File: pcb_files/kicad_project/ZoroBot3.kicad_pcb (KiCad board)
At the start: 2 copper layers, 67.6 x 91.9 mm, 178 parts, among them Q1 NMOS, Q2 AON7423, Q3 ST-1KL3A, Q4 ST-1KL3A, Q5 ST-1KL3A, Q6 ST-1KL3A, U1 MPU-6500, U2 MPU-6500, Y1 Crystal

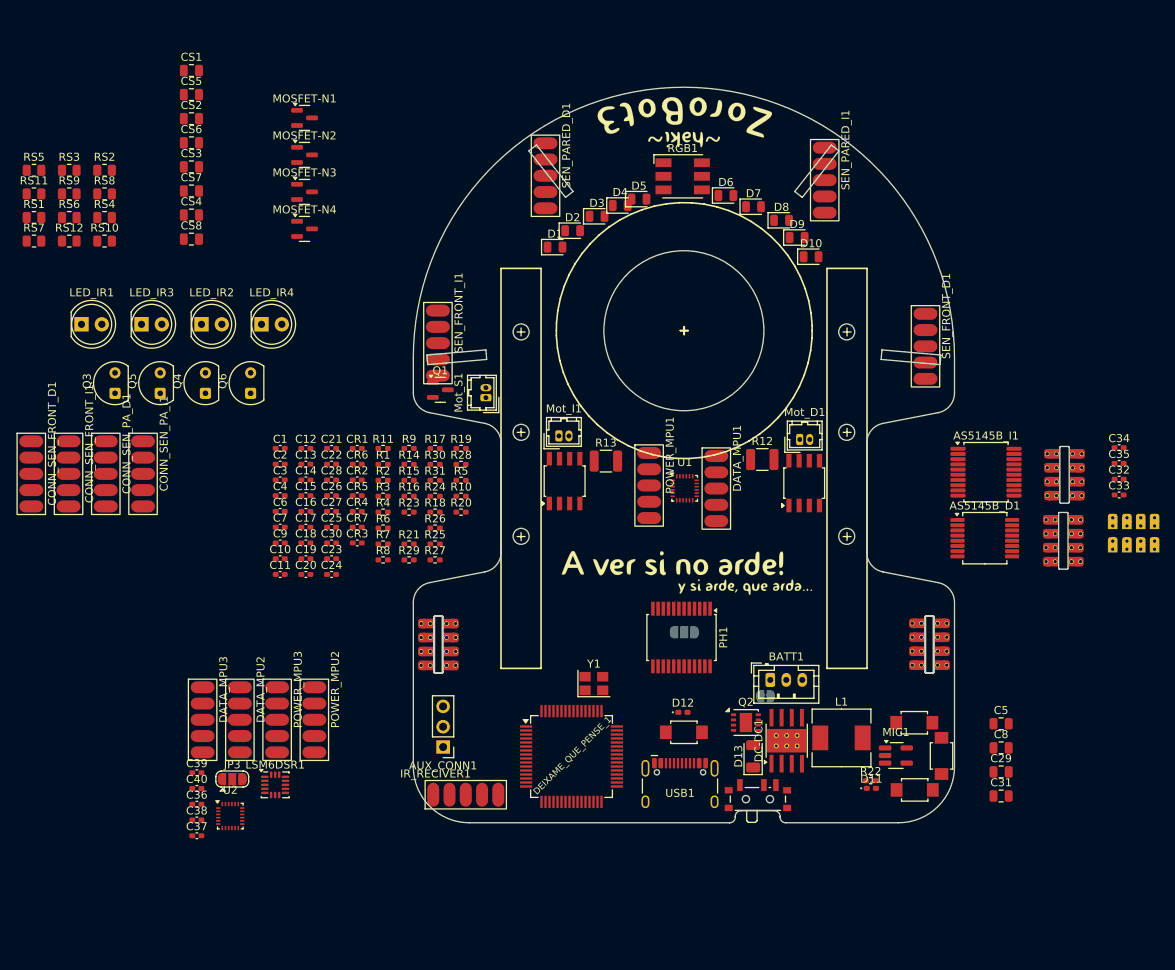
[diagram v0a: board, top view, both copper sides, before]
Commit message: Corrige errores de esquematico, crea las PCBs auxiliares, y posiciona todos los elementos para comenzar el ruteado.
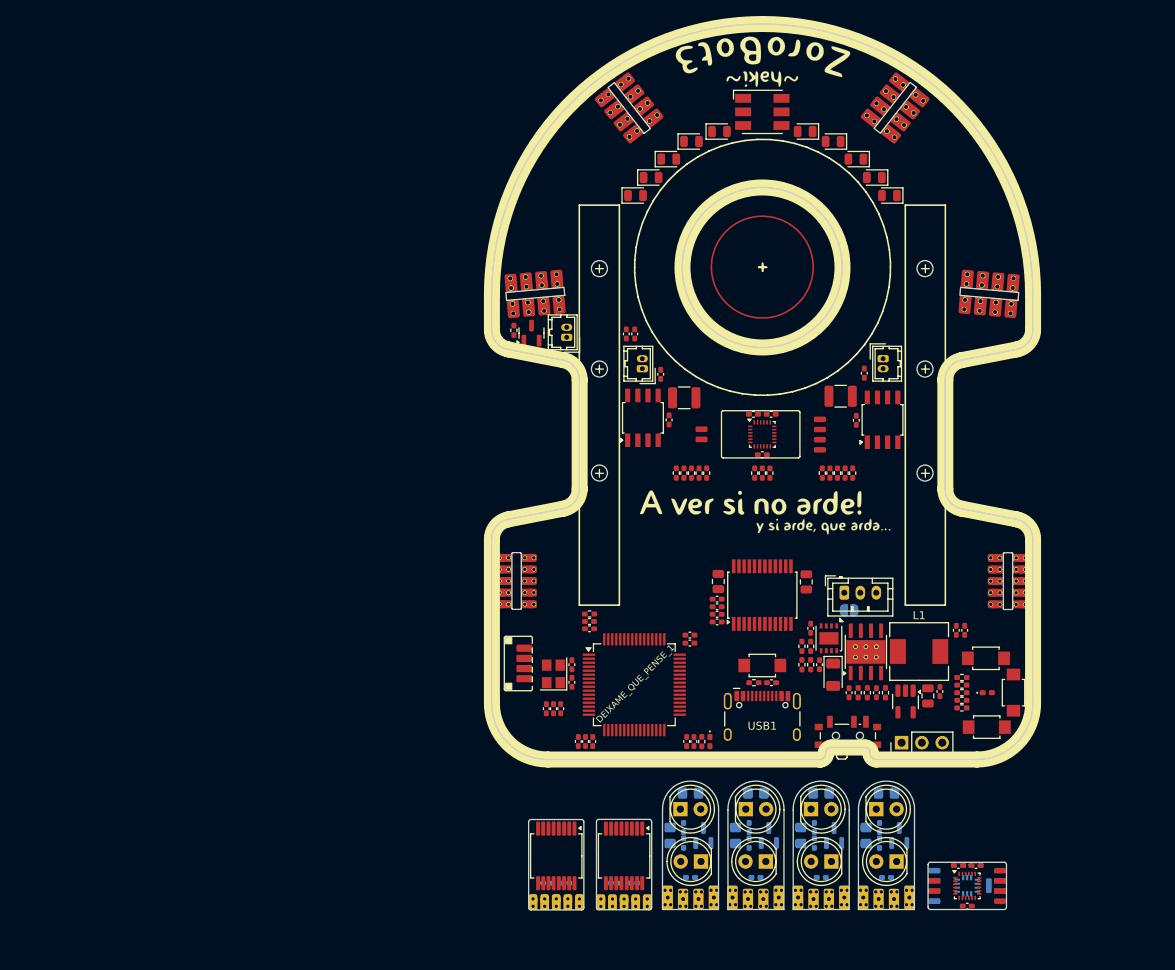
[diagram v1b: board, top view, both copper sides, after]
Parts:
- removed ENC_L1, ENC_R1: Conn_01x05_Socket, custom_footprints:FujitoraBot2_PCBmain_Encoder
- removed JP1: SolderJumper_3_Open, Jumper:SolderJumper-3_P1.3mm_Open_RoundedPad1.0x1.5mm
- AS5145B_I1: footprint Package_SO:SSOP-20_5.3x7.2mm_P0.65mm -> Package_SO:SSOP-16_5.3x6.2mm_P0.65mm
- C28: value 10uF -> 0.1uf
- C29: value 47uF -> 0.1uF; footprint Capacitor_SMD:C_0805_2012Metric -> Capacitor_SMD:C_0402_1005Metric_Pad0.74x0.62mm_HandSolder
- C32, C33, C34, C35, C37, C38, MOSFET-N1, MOSFET-N2, MOSFET-N3, MOSFET-N4: moved to B.Cu
- CONN_SEN_FRONT_D1, CONN_SEN_FRONT_I1, CONN_SEN_PA_D1, CONN_SEN_PA_I1: footprint custom_footprints:1x05 Pad -> custom_footprints:ZoroBot3_Sensors
- CS1, CS2, CS3, CS4, CS5, CS6, CS7, CS8: footprint Capacitor_SMD:C_0805_2012Metric -> Capacitor_SMD:C_0402_1005Metric_Pad0.74x0.62mm_HandSolder; moved to B.Cu
- DATA_MPU1, DATA_MPU3: footprint custom_footprints:1x05 Pad -> custom_footprints:ZoroBot3_Data_MPU
- DATA_MPU2: footprint custom_footprints:1x05 Pad -> custom_footprints:ZoroBot3_Data_MPU; moved to B.Cu
- ENC_D1, ENC_I1: footprint custom_footprints:FujitoraBot2_PCBmain_Encoder -> custom_footprints:ZoroBot3_PCBmain_Encoder
- ENC_D_CONN1, ENC_I_CONN1: footprint custom_footprints:FujitoraBot2_PCBmodule_encoder -> custom_footprints:ZoroBot3_PCBmodule_encoder
- IR_RECIVER1: footprint custom_footprints:1x05 Pad -> custom_footprints:IR_SENSOR_SMD_TSSP77038ETR
- JP3: value SolderJumper_3_Open -> Conn_01x01_Pin; footprint Jumper:SolderJumper-3_P1.3mm_Open_RoundedPad1.0x1.5mm -> custom_footprints:Generic_simple_1x_SMD_pin; moved to B.Cu
- LED_IR1, LED_IR2, LED_IR3, LED_IR4: footprint LED_THT:LED_D5.0mm -> LED_THT:LED_D5.0mm_Clear
- LSM6DSR1: footprint Sensor_Motion:Analog_LGA-16_3.25x3mm_P0.5mm_LayoutBorder3x5y -> Package_LGA:Bosch_LGA-14_3x2.5mm_P0.5mm; moved to B.Cu
- Mot_D1, Mot_I1, Mot_S1: footprint Connector_Hirose:Hirose_DF13-02P-1.25DSA_1x02_P1.25mm_Vertical -> custom_footprints:Connector_motor_1.25_Hirose_DF13-02P-1.25DSA_1x02_P1.25mm_Vertical
- POWER_MPU1, POWER_MPU2: footprint custom_footprints:1x05 Pad -> custom_footprints:ZoroBot3_Power_MPU
- POWER_MPU3: footprint custom_footprints:1x05 Pad -> custom_footprints:ZoroBot3_Power_MPU; moved to B.Cu
- Q3, Q4, Q5, Q6: footprint OptoDevice:Osram_SFH205 -> LED_THT:LED_D5.0mm_IRBlack
- RS1, RS10, RS2, RS3, RS4, RS7, RS8, RS9: footprint Resistor_SMD:R_0805_2012Metric -> Resistor_SMD:R_0805_2012Metric_Pad1.20x1.40mm_HandSolder; moved to B.Cu
- RS11, RS12, RS5, RS6: footprint Resistor_SMD:R_0805_2012Metric -> Resistor_SMD:R_0402_1005Metric_Pad0.72x0.64mm_HandSolder; moved to B.Cu
- SEN_FRONT_D1, SEN_FRONT_I1, SEN_PARED_D1, SEN_PARED_I1: footprint custom_footprints:1x05 Pad -> custom_footprints:ZoroBot3_Main_sensors
- Y1: value Crystal -> Crystal_GND24
- moved RS5 135.1 mm to (165.8, 134.4), turned to 90 degrees
- moved RS3 129.7 mm to (164.1, 133.4), turned to 90 degrees
- moved CS2 128.6 mm to (166.6, 138.7), turned to 180 degrees
- moved RS1 128.6 mm to (166.6, 128.2)
- moved CS1 127.9 mm to (165.8, 132.4), turned to -90 degrees
- moved RS11 126.9 mm to (157.6, 134.4), turned to 90 degrees
- moved RS9 121.6 mm to (155.9, 133.4), turned to 90 degrees
- moved CS6 121.0 mm to (158.5, 138.7), turned to 180 degrees
- moved CS5 120.2 mm to (157.6, 132.4), turned to -90 degrees
- moved RS7 120.2 mm to (158.5, 128.2)
- moved MOSFET-N1 116.5 mm to (168.2, 133.4), turned to 90 degrees
- moved LED_IR1 116.4 mm to (165.3, 130.2)
- moved CONN_SEN_FRONT_D1 115.6 mm to (159.6, 141.2)
- moved CONN_SEN_PA_D1 114.5 mm to (167.8, 141.2)
- moved Q3 113.9 mm to (167.9, 136.7), turned to 180 degrees
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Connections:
- CS1 pad 1: Net-(LED_IR1-A) -> /Sensores/3.3_D
- CS3 pad 1: Net-(LED_IR2-A) -> /Sensores/3.3_I
- CS5 pad 1: Net-(LED_IR3-A) -> /Sensores/3.3_FD
- CS7 pad 1: Net-(LED_IR4-A) -> /Sensores/3.3_FI
- JP3 pad 1: /Giroscopio/GND_MPU -> Net-(JP3-Pin_1)
- LSM6DSR1 pad 2: Net-(JP3-C) -> Net-(JP3-Pin_1)
- LSM6DSR1 pad 3: Net-(JP3-C) -> Net-(JP3-Pin_1)
- PH1 pad 6: Net-(JP1-C) -> +3V3
- Y1 pad 2: Net-(DEIXAME_QUE_PENSE_1-PH0/OSC_IN) -> GND
- Y1 pad 3: (no net) -> Net-(DEIXAME_QUE_PENSE_1-PH0/OSC_IN)
- Y1 pad 4: (no net) -> GND
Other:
- board size 67.6 x 91.9 mm -> 67.6 x 110.7 mm
- board text added: "Component"
- board text added: "Directly Below"
- board text added: "KEEPOUT"
- board text added: "No Copper"

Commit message: Finaliza el diseño de la PCB de ZoroBot3 Rebuild y añade gerbers y BOM
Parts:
- removed C14, C16: 0.1uF, Capacitor_SMD:C_0402_1005Metric_Pad0.74x0.62mm_HandSolder
- added C41: 10uF, Capacitor_SMD:C_0402_1005Metric_Pad0.74x0.62mm_HandSolder, F.Cu at (144.9, 119.4)
- added C42: 10uF, Capacitor_SMD:C_0402_1005Metric_Pad0.74x0.62mm_HandSolder, F.Cu at (144.9, 120.4)
- added C43: 10uF, Capacitor_SMD:C_0402_1005Metric_Pad0.74x0.62mm_HandSolder, F.Cu at (144.9, 121.4)
- added C44: 10uF, Capacitor_SMD:C_0402_1005Metric_Pad0.74x0.62mm_HandSolder, F.Cu at (170.6, 137.1)
- added C45: 10uF, Capacitor_SMD:C_0402_1005Metric_Pad0.74x0.62mm_HandSolder, F.Cu at (170.6, 135.2)
- added C46: 10uF, Capacitor_SMD:C_0402_1005Metric_Pad0.74x0.62mm_HandSolder, F.Cu at (170.6, 136.2)
- added C47: 10uF, Capacitor_SMD:C_0402_1005Metric_Pad0.74x0.62mm_HandSolder, F.Cu at (173.0, 124.9)
- added C48: 10uF, Capacitor_SMD:C_0402_1005Metric_Pad0.74x0.62mm_HandSolder, F.Cu at (170.9, 124.9)
- added C49: 10uF, Capacitor_SMD:C_0402_1005Metric_Pad0.74x0.62mm_HandSolder, F.Cu at (172.0, 124.9)
- added C50: 10uF, Capacitor_SMD:C_0402_1005Metric_Pad0.74x0.62mm_HandSolder, F.Cu at (168.9, 124.9)
- added C51: 10uF, Capacitor_SMD:C_0402_1005Metric_Pad0.74x0.62mm_HandSolder, F.Cu at (169.9, 124.9)
- added C52: 10uF, Capacitor_SMD:C_0402_1005Metric_Pad0.74x0.62mm_HandSolder, F.Cu at (170.6, 138.1)
- added kibuzzard-6779A98A: G***, kibuzzard-6779A98A, B.Cu at (110.8, 99.0)
- added kibuzzard-6779A9B1: G***, kibuzzard-6779A9B1, B.Cu at (185.3, 98.9)
- added kibuzzard-677A7C8F: G***, kibuzzard-677A7C8F, F.Cu at (155.8, 62.7)
- added kibuzzard-677A7C9A: G***, kibuzzard-677A7C9A, F.Cu at (159.0, 64.0)
- added kibuzzard-677A7CA3: G***, kibuzzard-677A7CA3, F.Cu at (161.9, 65.9)
- added kibuzzard-677A7CAF: G***, kibuzzard-677A7CAF, F.Cu at (164.4, 68.3)
- added kibuzzard-677A7CBB: G***, kibuzzard-677A7CBB, F.Cu at (166.3, 71.2)
- added kibuzzard-677A7D71: G***, kibuzzard-677A7D71, F.Cu at (136.8, 68.3)
- added kibuzzard-677A7D7B: G***, kibuzzard-677A7D7B, F.Cu at (139.2, 65.9)
- added kibuzzard-677A7D86: G***, kibuzzard-677A7D86, F.Cu at (142.1, 64.0)
- added kibuzzard-677A7E2E: G***, kibuzzard-677A7E2E, F.Cu at (134.8, 71.2)
- added kibuzzard-677A7E3B: G***, kibuzzard-677A7E3B, F.Cu at (145.3, 62.7)
- AS5145B_D1, AS5145B_I1: footprint Package_SO:SSOP-16_5.3x6.2mm_P0.65mm -> custom_footprints:Encoder_AS5145B
- BATT1: footprint Connector_JST:JST_PH_B3B-PH-K_1x03_P2.00mm_Vertical -> Connector_JST:JST_XH_B3B-XH-A_1x03_P2.50mm_Vertical
- C37, C38, DATA_MPU2, JP3, LSM6DSR1, POWER_MPU3: moved to F.Cu
- CR4, CR7: footprint Capacitor_SMD:C_0402_1005Metric_Pad0.74x0.62mm_HandSolder -> Capacitor_SMD:C_0603_1608Metric
- CR6: value 0.1uF -> 47uF; footprint Capacitor_SMD:C_0402_1005Metric_Pad0.74x0.62mm_HandSolder -> Capacitor_SMD:C_1206_3216Metric
- D13: footprint Diode_SMD:D_1206_3216Metric -> Diode_SMD:D_0805_2012Metric_Pad1.15x1.40mm_HandSolder
- MOSFET-N1, MOSFET-N2, MOSFET-N3, MOSFET-N4: value AO3401 -> AO3400 (A09T)
- R12, R13: footprint Resistor_SMD:R_1210_3225Metric -> Resistor_SMD:R_2512_6332Metric
- moved DATA_MPU3 79.3 mm to (113.3, 98.1), turned to 90 degrees
- moved C40 77.5 mm to (110.3, 102.2), turned to 90 degrees
- moved POWER_MPU3 75.3 mm to (113.3, 106.3), turned to 90 degrees
- moved U2 73.7 mm to (113.3, 102.2), turned to -90 degrees
- moved C39 71.3 mm to (116.4, 101.0), turned to 90 degrees
- moved C36 68.3 mm to (116.4, 103.2), turned to -90 degrees
- moved C33 65.4 mm to (178.9, 103.4), turned to 180 degrees
- moved AS5145B_D1 64.2 mm to (178.9, 100.7)
- moved ENC_D_CONN1 63.6 mm to (178.9, 106.3)
- moved C32 63.1 mm to (178.9, 104.4)
- moved RS9 62.5 mm to (188.2, 79.9)
- moved CONN_SEN_PA_I1 62.3 mm to (111.2, 87.8)
- moved MOSFET-N2 62.2 mm to (112.2, 79.9)
- moved LED_IR3 62.1 mm to (188.6, 76.6)
- moved RS7 62.1 mm to (189.9, 74.6)
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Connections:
- AD8418AWBZ_2 pad 1: /SHUNT_MI -> /MOT_I-
- AD8418AWBZ_2 pad 8: /MOT_I+ -> /SHUNT_MI
- C36 pad 1: /Giroscopio/GND_MPU -> /Giroscopio/GND_MPU_A
- C36 pad 2: /Giroscopio/3.3_MPU -> /Giroscopio/3.3_MPU_A
- C37 pad 1: /Giroscopio/GND_MPU -> /Giroscopio/GND_MPU_B
- C37 pad 2: /Giroscopio/3.3_MPU -> /Giroscopio/3.3_MPU_B
- C38 pad 1: /Giroscopio/GND_MPU -> /Giroscopio/GND_MPU_B
- C38 pad 2: /Giroscopio/3.3_MPU -> /Giroscopio/3.3_MPU_B
- C39 pad 1: /Giroscopio/GND_MPU -> /Giroscopio/GND_MPU_A
- C39 pad 2: /Giroscopio/3.3_MPU -> /Giroscopio/3.3_MPU_A
- C40 pad 1: /Giroscopio/GND_MPU -> /Giroscopio/GND_MPU_A
- DATA_MPU2 pad 1: /Giroscopio/SPI_MISO_CONN -> /Giroscopio/SPI_MISO_CONN_B
- DATA_MPU2 pad 2: /Giroscopio/SPI_MOSI_CONN -> /Giroscopio/SPI_MOSI_CONN_B
- DATA_MPU2 pad 3: /Giroscopio/SPI_SCK_CONN -> /Giroscopio/SPI_SCK_CONN_B
- DATA_MPU2 pad 4: /Giroscopio/SPI_NSS_CONN -> /Giroscopio/SPI_NSS_CONN_B
- DATA_MPU3 pad 1: /Giroscopio/SPI_MISO_CONN -> /Giroscopio/SPI_MISO_CONN_A
- DATA_MPU3 pad 2: /Giroscopio/SPI_MOSI_CONN -> /Giroscopio/SPI_MOSI_CONN_A
- DATA_MPU3 pad 3: /Giroscopio/SPI_SCK_CONN -> /Giroscopio/SPI_SCK_CONN_A
- DATA_MPU3 pad 4: /Giroscopio/SPI_NSS_CONN -> /Giroscopio/SPI_NSS_CONN_A
- DEIXAME_QUE_PENSE_1 pad 54: /ENC_2_I -> /ENC_D_I
- DEIXAME_QUE_PENSE_1 pad 55: /ENC_1_I -> /ENC_I_I
- DEIXAME_QUE_PENSE_1 pad 56: /ENC_2_B -> /ENC_D_B
- DEIXAME_QUE_PENSE_1 pad 57: /ENC_2_A -> /ENC_D_A
- DEIXAME_QUE_PENSE_1 pad 58: /ENC_1_B -> /ENC_I_B
- DEIXAME_QUE_PENSE_1 pad 59: /ENC_1_A -> /ENC_I_A
- ENC_D1 pad 3: /ENC_1_A -> /ENC_D_I
- ENC_D1 pad 4: /ENC_1_B -> /ENC_D_A
- ENC_D1 pad 5: /ENC_1_I -> /ENC_D_B
- ENC_D_CONN1 pad 3: /Encoders/ENC_D_A_CONN -> /Encoders/ENC_D_I_CONN
- ENC_D_CONN1 pad 4: /Encoders/ENC_D_B_CONN -> /Encoders/ENC_D_A_CONN
- ENC_D_CONN1 pad 5: /Encoders/ENC_D_I_CONN -> /Encoders/ENC_D_B_CONN
- ENC_I1 pad 3: /ENC_2_A -> /ENC_I_I
- ENC_I1 pad 4: /ENC_2_B -> /ENC_I_A
- ENC_I1 pad 5: /ENC_2_I -> /ENC_I_B
- ENC_I_CONN1 pad 3: /Encoders/ENC_I_A_CONN -> /Encoders/ENC_I_I_CONN
- ENC_I_CONN1 pad 4: /Encoders/ENC_I_B_CONN -> /Encoders/ENC_I_A_CONN
- ENC_I_CONN1 pad 5: /Encoders/ENC_I_I_CONN -> /Encoders/ENC_I_B_CONN
- LSM6DSR1 pad 1: /Giroscopio/SPI_MISO_CONN -> /Giroscopio/SPI_MISO_CONN_B
- LSM6DSR1 pad 12: /Giroscopio/SPI_NSS_CONN -> /Giroscopio/SPI_NSS_CONN_B
- LSM6DSR1 pad 13: /Giroscopio/SPI_SCK_CONN -> /Giroscopio/SPI_SCK_CONN_B
- LSM6DSR1 pad 14: /Giroscopio/SPI_MOSI_CONN -> /Giroscopio/SPI_MOSI_CONN_B
- LSM6DSR1 pad 5: /Giroscopio/3.3_MPU -> /Giroscopio/3.3_MPU_B
- LSM6DSR1 pad 6: /Giroscopio/GND_MPU -> /Giroscopio/GND_MPU_B
- LSM6DSR1 pad 7: /Giroscopio/GND_MPU -> /Giroscopio/GND_MPU_B
- LSM6DSR1 pad 8: /Giroscopio/3.3_MPU -> /Giroscopio/3.3_MPU_B
- MOSFET-N1 pad 1: /Sensores/EMI_PA_D_CONN -> Net-(LED_IR1-K)
- MOSFET-N1 pad 2: /Sensores/GND_D -> /Sensores/EMI_PA_D_CONN
- MOSFET-N1 pad 3: Net-(LED_IR1-K) -> /Sensores/GND_D
- MOSFET-N2 pad 1: /Sensores/EMI_PA_I_CONN -> Net-(LED_IR2-K)
- MOSFET-N2 pad 2: /Sensores/GND_I -> /Sensores/EMI_PA_I_CONN
- MOSFET-N2 pad 3: Net-(LED_IR2-K) -> /Sensores/GND_I
- MOSFET-N3 pad 1: /Sensores/EMI_FRONT_D_CONN -> Net-(LED_IR3-K)
- MOSFET-N3 pad 2: /Sensores/GND_FD -> /Sensores/EMI_FRONT_D_CONN
- MOSFET-N3 pad 3: Net-(LED_IR3-K) -> /Sensores/GND_FD
- MOSFET-N4 pad 1: /Sensores/EMI_FRONT_I_CONN -> Net-(LED_IR4-K)
- MOSFET-N4 pad 2: /Sensores/GND_FI -> /Sensores/EMI_FRONT_I_CONN
- MOSFET-N4 pad 3: Net-(LED_IR4-K) -> /Sensores/GND_FI
- PH1 pad 1: /BATT -> /SHUNT_MD
- PH1 pad 10: /MOT_I_PWM -> GND
- PH1 pad 11: /BATT -> /SHUNT_MI
- PH1 pad 12: /BATT -> /SHUNT_MI
- PH1 pad 13: /SHUNT_MI -> /BATT
- PH1 pad 14: /SHUNT_MI -> /BATT
- PH1 pad 15: GND -> /MOT_I_PWM
- PH1 pad 16: GND -> /MOT_I_B
- PH1 pad 17: /MOT_I- -> /MOT_I_A
- PH1 pad 18: /MOT_I- -> GND
- PH1 pad 19: /MOT_D- -> +3V3
- PH1 pad 2: /MOT_D_PWM -> /SHUNT_MD
- PH1 pad 20: /MOT_D- -> +3V3
- PH1 pad 21: GND -> /MOT_D_B
- PH1 pad 22: GND -> /MOT_D_A
- PH1 pad 23: /SHUNT_MD -> /MOT_D_PWM
- PH1 pad 24: /SHUNT_MD -> /BATT
- PH1 pad 3: /MOT_D_A -> GND
- PH1 pad 4: /MOT_D_B -> GND
- PH1 pad 5: +3V3 -> /MOT_D-
- PH1 pad 6: +3V3 -> /MOT_D-
- PH1 pad 7: GND -> /MOT_I+
- PH1 pad 8: /MOT_I_A -> /MOT_I+
- PH1 pad 9: /MOT_I_B -> GND
- POWER_MPU2 pad 1: /Giroscopio/GND_MPU -> /Giroscopio/GND_MPU_B
- POWER_MPU2 pad 2: /Giroscopio/3.3_MPU -> /Giroscopio/3.3_MPU_B
- POWER_MPU3 pad 1: /Giroscopio/GND_MPU -> /Giroscopio/GND_MPU_A
- POWER_MPU3 pad 2: /Giroscopio/3.3_MPU -> /Giroscopio/3.3_MPU_A
- POWER_SWITCH1 pad 1: unconnected-(POWER_SWITCH1-A-Pad1) -> Net-(POWER_SWITCH1-A)
- POWER_SWITCH1 pad 3: Net-(POWER_SWITCH1-C) -> unconnected-(POWER_SWITCH1-C-Pad3)
- R13 pad 1: /MOT_I+ -> /MOT_I-
- R27 pad 1: Net-(POWER_SWITCH1-C) -> Net-(POWER_SWITCH1-A)
- R28 pad 1: Net-(POWER_SWITCH1-C) -> Net-(POWER_SWITCH1-A)
- U2 pad 13: /Giroscopio/3.3_MPU -> /Giroscopio/3.3_MPU_A
- U2 pad 18: /Giroscopio/GND_MPU -> /Giroscopio/GND_MPU_A
- U2 pad 20: /Giroscopio/GND_MPU -> /Giroscopio/GND_MPU_A
- U2 pad 22: /Giroscopio/SPI_NSS_CONN -> /Giroscopio/SPI_NSS_CONN_A
- U2 pad 23: /Giroscopio/SPI_SCK_CONN -> /Giroscopio/SPI_SCK_CONN_A
- U2 pad 24: /Giroscopio/SPI_MOSI_CONN -> /Giroscopio/SPI_MOSI_CONN_A
- U2 pad 8: /Giroscopio/3.3_MPU -> /Giroscopio/3.3_MPU_A
- U2 pad 9: /Giroscopio/SPI_MISO_CONN -> /Giroscopio/SPI_MISO_CONN_A
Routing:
- net +3V3: track 0.00 -> 804.2 mm, vias 0 -> 35
- net GND: track 0.00 -> 289.1 mm, vias 0 -> 130
- net +5V: track 0.00 -> 164.6 mm, vias 0 -> 20
- net /EMI_FRONT_D: track 0.00 -> 142.2 mm, vias 0 -> 4
- net /SEN_FRONT_D: track 0.00 -> 141.4 mm, vias 0 -> 2
- net /EMI_PA_I: track 0.00 -> 136.3 mm, vias 0 -> 3
- net /SEN_PA_I: track 0.00 -> 132.6 mm, vias 0 -> 5
- net /BATT: track 0.00 -> 117.9 mm, vias 0 -> 34
- net /EMI_PA_D: track 0.00 -> 117.1 mm, vias 0 -> 3
- net /SEN_PA_D: track 0.00 -> 106.3 mm, vias 0 -> 2
- net /EMI_FRONT_I: track 0.00 -> 101.2 mm, vias 0 -> 4
- net /SEN_FRONT_I: track 0.00 -> 99.5 mm, vias 0 -> 3
- net /MENU_ANALOG: track 0.00 -> 88.6 mm, vias 0 -> 6
- net /MOT_S_PWM: track 0.00 -> 86.8 mm, vias 0 -> 4
- net /AUX_PIN: track 0.00 -> 83.2 mm, vias 0 -> 1
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- added copper zone on B.Cu, net +3V3
- added copper zone on B.Cu, net +5V
- added copper zone on F.Cu, net +5V
- added copper zone on B.Cu, net /BATT
- added copper zone on F.Cu, net /BATT
- added copper zone on B.Cu, net /LIPO+
- added copper zone on F.Cu, net /LIPO+
- added copper zone on B.Cu, net GND
- added copper zone on F.Cu, net GND
- added copper zone on B.Cu, net Net-(DC-DC1-SW)
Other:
- board size 67.6 x 110.7 mm -> 85.8 x 91.9 mm
- board text added: "JLCJLCJLCJLC"
